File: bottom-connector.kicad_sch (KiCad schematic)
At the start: 6 parts, among them J1 Compute-Module-4_Plug_Connect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, Q3 DZDH0401DW, Q9 AO3401A

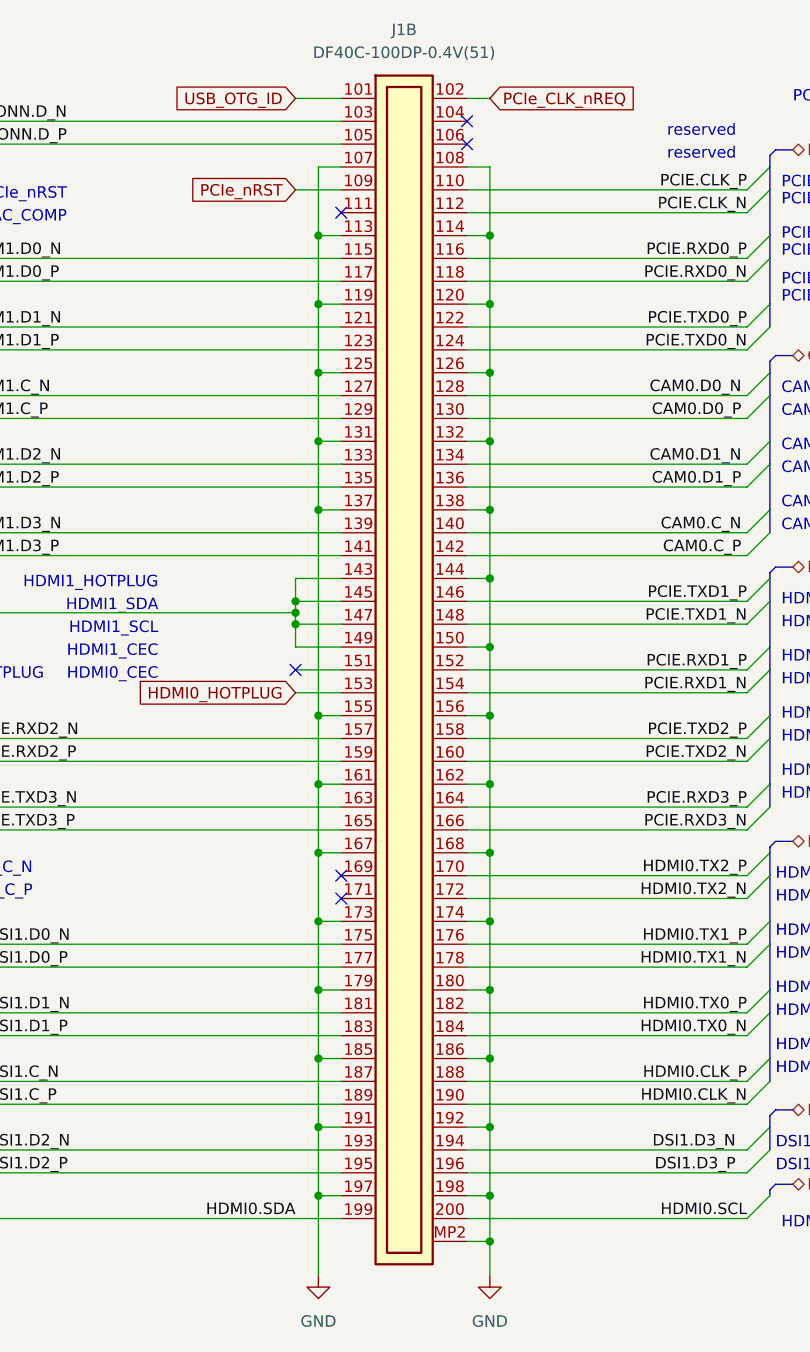
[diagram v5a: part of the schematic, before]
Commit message: [#59450] Remove custom CM4 connector, add CM4 outline with regular DF40C-100DP-0.4V(51) connectors
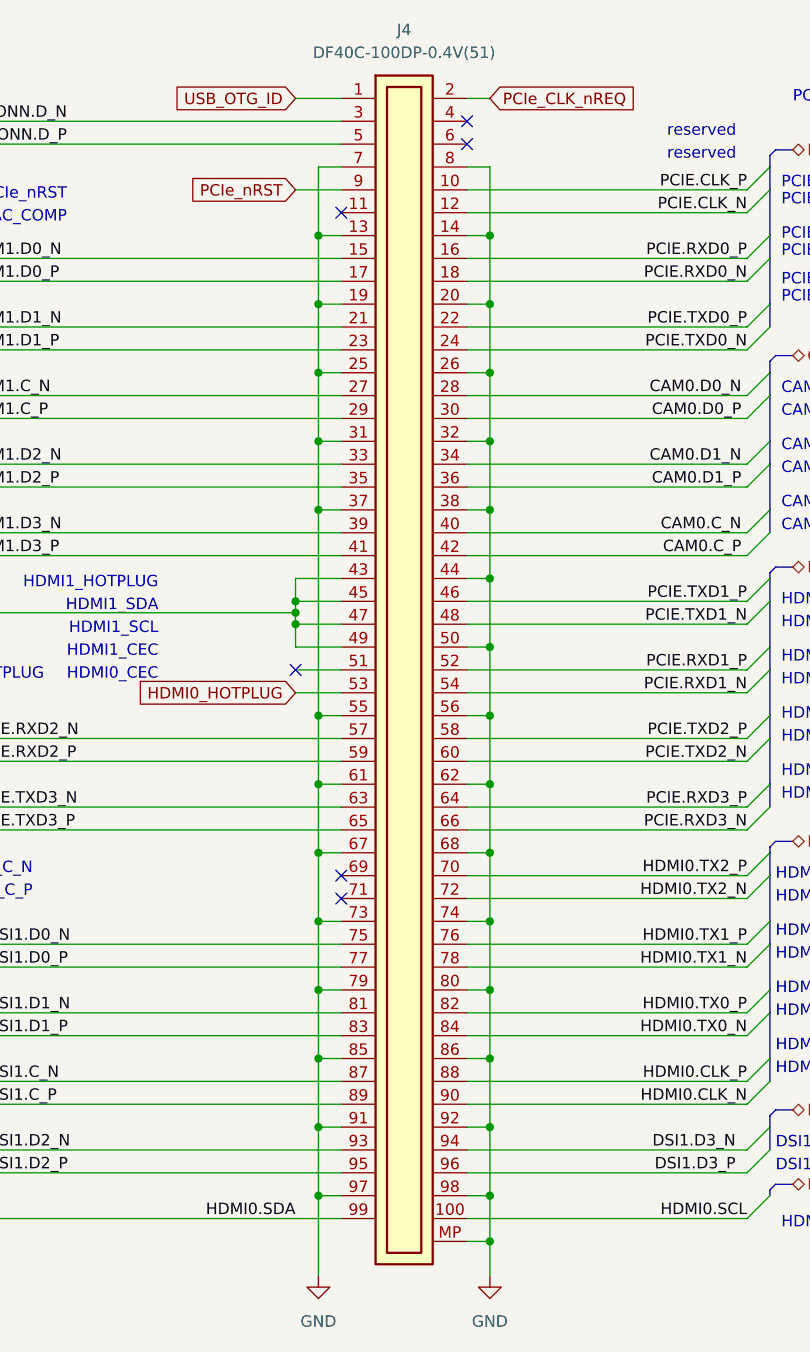
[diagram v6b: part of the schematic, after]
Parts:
- removed J1: Compute-Module-4_Plug_Connector, antmicro-footprints:Compute-Module-4_Plug_Connector, symbol antmicroModules:Compute-Module-4_Plug_Connector
- added J4: Plug_Hirose_DF40_2x50_DF40C-100DP-0.4V, antmicro-footprints:Conn_Plug_Hirose_DF40_2x50_DF40C-100DP-0.4V, symbol antmicroB2BConnectors:Plug_Hirose_DF40_2x50_DF40C-100DP-0.4V
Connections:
- net CAM0.C_N: now also J4.40
- net CAM0.C_P: now also J4.42
- net CAM0.D0_N: now also J4.28
- net CAM0.D0_P: now also J4.30
- net CAM0.D1_N: now also J4.34
- net CAM0.D1_P: now also J4.36
- net CAM1.C_N: now also J4.27
- net CAM1.C_P: now also J4.29
- net CAM1.D0_N: now also J4.15
- net CAM1.D0_P: now also J4.17
- net CAM1.D1_N: now also J4.21
- net CAM1.D1_P: now also J4.23
- net CAM1.D2_N: now also J4.33
- net CAM1.D2_P: now also J4.35
- net CAM1.D3_N: now also J4.39
- net CAM1.D3_P: now also J4.41
- net CONN.D_N: now also J4.3
- net CONN.D_P: now also J4.5
- net DSI1.C_N: now also J4.87
- net DSI1.C_P: now also J4.89
- net DSI1.D0_N: now also J4.75
- net DSI1.D0_P: now also J4.77
- net DSI1.D1_N: now also J4.81
- net DSI1.D1_P: now also J4.83
- net DSI1.D2_N: now also J4.93
- net DSI1.D2_P: now also J4.95
- net DSI1.D3_N: now also J4.94
- net DSI1.D3_P: now also J4.96
- net GND: now also J4.13, J4.14, J4.19, J4.20, J4.25, J4.26, J4.31, J4.32, J4.37, J4.38, J4.44, J4.50, J4.55, J4.56, J4.61, J4.62, J4.67, J4.68, J4.7, J4.73, J4.74, J4.79, J4.8, J4.80, J4.85, J4.86, J4.91, J4.92, J4.97, J4.98, J4.MP
- net HDMI0.CLK_N: now also J4.90
- net HDMI0.CLK_P: now also J4.88
- net HDMI0.SCL: now also J4.100
- net HDMI0.SDA: now also J4.99
- net HDMI0.TX0_N: now also J4.84
- net HDMI0.TX0_P: now also J4.82
- net HDMI0.TX1_N: now also J4.78
- net HDMI0.TX1_P: now also J4.76
- net HDMI0.TX2_N: now also J4.72
- net HDMI0.TX2_P: now also J4.70
- net HDMI0_HOTPLUG: now also J4.53
- net PCIE.CLK_N: now also J4.12
- net PCIE.CLK_P: now also J4.10
- net PCIE.RXD0_N: now also J4.18
- net PCIE.RXD0_P: now also J4.16
- net PCIE.RXD1_N: now also J4.54
- net PCIE.RXD1_P: now also J4.52
- net PCIE.RXD2_N: now also J4.57
- net PCIE.RXD2_P: now also J4.59
- net PCIE.RXD3_N: now also J4.66
- net PCIE.RXD3_P: now also J4.64
- net PCIE.TXD0_N: now also J4.24
- net PCIE.TXD0_P: now also J4.22
- net PCIE.TXD1_N: now also J4.48
- net PCIE.TXD1_P: now also J4.46
- net PCIE.TXD2_N: now also J4.60
- net PCIE.TXD2_P: now also J4.58
- net PCIE.TXD3_N: now also J4.63
- net PCIE.TXD3_P: now also J4.65
- net PCIe_CLK_nREQ: now also J4.2
- net PCIe_nRST: now also J4.9
- net USB_OTG_ID: now also J4.1
- net at Q3.6 (D), Q9.3 (D), R62.2: now also J4.43, J4.45, J4.47, J4.49
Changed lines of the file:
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@@
-    )
-  )
-  (symbol (lib_id "antmicroModules:Compute-Module-4_Plug_Connector") (at 227.33 77.47 0) (unit 2)
-    (in_bom yes) (on_board yes) (dnp no) (fields_autoplaced)
-    (property "Reference" "J1" (at 234.315 69.85 0)
-      (effects (font (size 1.27 1.27) (thickness 0.15)))
-    )
-    (property "Value" "Compute-Module-4_Plug_Connector" (at 250.19 80.645 0)
-      (effects (font (size 1.27 1.27) (thickness 0.15)) (justify left bottom) hide)
-    )
-    (property "Footprint" "antmicro-footprints:Compute-Module-4_Plug_Connector" (at 250.19 83.185 0)
-      (effects (font (size 1.27 1.27) (thickness 0.15)) (justify left bottom) hide)
-    )
-    (property "Datasheet" "https://www.hirose.com/en/product/document?clcode=CL0684-4032-1-51&productname=DF40C-100DP-0.4V(51)&series=DF40&documenttype=2DDrawing&lang=en&documentid=0001001212" (at 250.19 85.725 0)
-      (effects (font (size 1.27 1.27) (thickness 0.15)) (justify left bottom) hide)
-    )
-    (property "MPN" "DF40C-100DP-0.4V(51)" (at 234.315 72.39 0)
-      (effects (font (size 1.27 1.27) (thickness 0.15)))
-    )
-    (property "Manufacturer" "Hirose Electric" (at 250.19 88.265 0)
-      (effects (font (size 1.27 1.27) (thickness 0.15)) (justify left bottom) hide)
-    )
-    (property "Pitch" "0.4 mm" (at 250.19 90.805 0)
-      (effects (font (size 1.27 1.27)) (justify left bottom) hide)
-    )
-    (property "Author" "Antmicro" (at 250.19 93.345 0)
-      (effects (font (size 1.27 1.27) (thickness 0.15)) (justify left bottom) hide)
-    )
-    (property "License" "Apache-2.0" (at 250.19 95.885 0)
-      (effects (font (size 1.27 1.27) (thickness 0.15)) (justify left bottom) hide)
-    )
-    (pin "1")
-    (pin "10")
-    (pin "100")
-    (pin "11")
-    (pin "12")
-    (pin "13")
-    (pin "14")
-    (pin "15")
-    (pin "16")
-    (pin "17")
-    (pin "18")
-    (pin "19")
-    (pin "2")
-    (pin "20")
-    (pin "21")
-    (pin "22")
-    (pin "23")
-    (pin "24")
-    (pin "25")
-    (pin "26")
-    (pin "27")
-    (pin "28")
-    (pin "29")
-    (pin "3")
-    (pin "30")
-    (pin "31")
-    (pin "32")
-    (pin "33")
-    (pin "34")
-    (pin "35")
-    (pin "36")
-    (pin "37")
-    (pin "38")
-    (pin "39")
-    (pin "4")
-    (pin "40")
-    (pin "41")
-    (pin "42")
-    (pin "43")
-    (pin "44")
-    (pin "45")
-    (pin "46")
-    (pin "47")
-    (pin "48")
-    (pin "49")
-    (pin "5")
-    (pin "50")
-    (pin "51")
-    (pin "52")
-    (pin "53")
-    (pin "54")
-    (pin "55")
-    (pin "56")
-    (pin "57")
-    (pin "58")
-    (pin "59")
-    (pin "6")
-    (pin "60")
-    (pin "61")
-    (pin "62")
-    (pin "63")
-    (pin "64")
-    (pin "65")
-    (pin "66")
-    (pin "67")
-    (pin "68")
-    (pin "69")
-    (pin "7")
-    (pin "70")
-    (pin "71")
-    (pin "72")
-    (pin "73")
-    (pin "74")
-    (pin "75")
-    (pin "76")
-    (pin "77")
-    (pin "78")
-    (pin "79")
-    (pin "8")
-    (pin "80")
-    (pin "81")
-    (pin "82")
-    (pin "83")
-    (pin "84")
-    (pin "85")
-    (pin "86")
-    (pin "87")
-    (pin "88")
-    (pin "89")
-    (pin "9")
-    (pin "90")
-    (pin "91")
-    (pin "92")
-    (pin "93")
-    (pin "94")
-    (pin "95")
-    (pin "96")
-    (pin "97")
-    (pin "98")
-    (pin "99")
-    (pin "MP1")
-    (pin "101")
-    (pin "102")
-    (pin "103")
-    (pin "104")
-    (pin "105")
-    (pin "106")
-    (pin "107")
-    (pin "108")
-    (pin "109")
-    (pin "110")
-    (pin "111")
-    (pin "112")
-    (pin "113")
-    (pin "114")
-    (pin "115")
-    (pin "116")
-    (pin "117")
-    (pin "118")
-    (pin "119")
-    (pin "120")
-    (pin "121")
-    (pin "122")
-    (pin "123")
-    (pin "124")
-    (pin "125")
-    (pin "126")
-    (pin "127")
-    (pin "128")
-    (pin "129")
-    (pin "130")
-    (pin "131")
-    (pin "132")
-    (pin "133")
-    (pin "134")
-    (pin "135")
-    (pin "136")
-    (pin "137")
-    (pin "138")
-    (pin "139")
-    (pin "140")
-    (pin "141")
-    (pin "142")
-    (pin "143")
-    (pin "144")
-    (pin "145")
-    (pin "146")
-    (pin "147")
-    (pin "148")
-    (pin "149")
-    (pin "150")
-    (pin "151")
-    (pin "152")
-    (pin "153")
-    (pin "154")
-    (pin "155")
-    (pin "156")
-    (pin "157")
-    (pin "158")
-    (pin "159")
-    (pin "160")
-    (pin "161")
-    (pin "162")
-    (pin "163")
-    (pin "164")
-    (pin "165")
-    (pin "166")
-    (pin "167")
-    (pin "168")
-    (pin "169")
-    (pin "170")
-    (pin "171")
-    (pin "172")
-    (pin "173")
-    (pin "174")
-    (pin "175")
-    (pin "176")
-    (pin "177")
-    (pin "178")
-    (pin "179")
-    (pin "180")
-    (pin "181")
-    (pin "182")
-    (pin "183")
-    (pin "184")
-    (pin "185")
-    (pin "186")
-    (pin "187")
-    (pin "188")
-    (pin "189")
-    (pin "190")
-    (pin "191")
-    (pin "192")
-    (pin "193")
-    (pin "194")
-    (pin "195")
-    (pin "196")
-    (pin "197")
-    (pin "198")
-    (pin "199")
-    (pin "200")
-    (pin "MP2")
-    (instances
-      (project "polarfire-som"
-        (path "/db4a0d3e-2eb3-499e-977d-6eb378cfd3ed/d540798e-a90a-44e1-a80e-8e0c2b3fef06"
-          (reference "J1") (unit 2)
-        )
-      )
     )
   )
@@
         )
       )
+    )
+  )
+  (symbol (lib_id "antmicroB2BConnectors:Plug_Hirose_DF40_2x50_DF40C-100DP-0.4V") (at 227.33 77.47 0) (unit 1)
+    (in_bom yes) (on_board yes) (dnp no) (fields_autoplaced)
+    (property "Reference" "J4" (at 234.315 69.85 0)
+      (effects (font (size 1.27 1.27) (thickness 0.15)))
+    )
+    (property "Value" "Plug_Hirose_DF40_2x50_DF40C-100DP-0.4V" (at 264.16 82.55 0)
+      (effects (font (size 1.27 1.27) (thickness 0.15)) (justify left bottom) hide)
+    )
+    (property "Footprint" "antmicro-footprints:Conn_Plug_Hirose_DF40_2x50_DF40C-100DP-0.4V" (at 264.16 85.09 0)
+      (effects (font (size 1.27 1.27) (thickness 0.15)) (justify left bottom) hide)
+    )
+    (property "Datasheet" "https://www.hirose.com/en/product/document?clcode=CL0684-4032-1-51&productname=DF40C-100DP-0.4V(51)&series=DF40&documenttype=2DDrawing&lang=en&documentid=0001001212" (at 264.16 87.63 0)
+      (effects (font (size 1.27 1.27) (thickness 0.15)) (justify left bottom) hide)
+    )
+    (property "MPN" "DF40C-100DP-0.4V(51)" (at 234.315 72.39 0)
+      (effects (font (size 1.27 1.27) (thickness 0.15)))
+    )
+    (property "Manufacturer" "Hirose Electric" (at 264.16 90.17 0)
+      (effects (font (size 1.27 1.27) (thickness 0.15)) (justify left bottom) hide)
+    )
+    (property "Pitch" "0.4 mm" (at 264.16 92.71 0)
+      (effects (font (size 1.27 1.27)) (justify left bottom) hide)
+    )
+    (property "Author" "Antmicro" (at 264.16 95.25 0)
+      (effects (font (size 1.27 1.27) (thickness 0.15)) (justify left bottom) hide)
+    )
+    (property "License" "Apache-2.0" (at 264.16 97.79 0)
+      (effects (font (size 1.27 1.27) (thickness 0.15)) (justify left bottom) hide)
+    )
+    (pin "53")
+    (pin "57")
+    (pin "89")
+    (pin "25")
+    (pin "67")
+    (pin "27")
+    (pin "56")
+    (pin "79")
+    (pin "29")
+    (pin "43")
+    (pin "93")
+    (pin "10")
+    (pin "20")
+    (pin "19")
+    (pin "41")
+    (pin "11")
+    (pin "100")
+    (pin "13")
+    (pin "18")
+    (pin "40")
+    (pin "12")
+    (pin "1")
+    (pin "22")
+    (pin "17")
+    (pin "80")
+    (pin "64")
+    (pin "26")
+    (pin "6")
+    (pin "87")
+    (pin "3")
+    (pin "52")
+    (pin "35")
+    (pin "55")
+    (pin "94")
+    (pin "76")
+    (pin "5")
+    (pin "73")
+    (pin "71")
+    (pin "47")
+    (pin "88")
+    (pin "95")
+    (pin "14")
+    (pin "MP")
+    (pin "99")
+    (pin "85")
+    (pin "84")
+    (pin "86")
+    (pin "24")
+    (pin "59")
+    (pin "90")
+    (pin "77")
+    (pin "78")
+    (pin "69")
+    (pin "65")
+    (pin "68")
+    (pin "74")
+    (pin "60")
+    (pin "72")
+    (pin "98")
+    (pin "66")
+    (pin "45")
+    (pin "58")
+    (pin "50")
+    (pin "61")
+    (pin "62")
+    (pin "44")
+    (pin "82")
+    (pin "2")
+    (pin "96")
+    (pin "42")
+    (pin "81")
+    (pin "63")
+    (pin "97")
+    (pin "15")
+    (pin "16")
+    (pin "21")
+    (pin "36")
+    (pin "38")
+    (pin "75")
+    (pin "70")
+    (pin "8")
+    (pin "9")
+    (pin "92")
+    (pin "32")
+    (pin "31")
+    (pin "39")
+    (pin "33")
+    (pin "51")
+    (pin "4")
+    (pin "54")
+    (pin "34")
+    (pin "37")
+    (pin "28")
+    (pin "30")
+    (pin "91")
+    (pin "23")
+    (pin "48")
+    (pin "83")
+    (pin "7")
+    (pin "49")
+    (pin "46")
+    (instances
+      (project "polarfire-som"
+        (path "/db4a0d3e-2eb3-499e-977d-6eb378cfd3ed/d540798e-a90a-44e1-a80e-8e0c2b3fef06"
+          (reference "J4") (unit 1)
+        )
+      )
